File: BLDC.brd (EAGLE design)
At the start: 75.9 x 65.4 mm, 131 parts, among them J3 1-770174-1, U1 MCP2562, U2 STM32F405RGT6, U3 DRV8302, U4 LM3671MF-3.3/NOPB, Y1 8MHz

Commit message: added stm32 LEDs
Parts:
- removed J3: 1-770174-1, FormE:CON4_2X2_P163_VMNL-1MTG
- removed R54, R55: 1k, adafruit:R0805
- added LED4: GREEN, FormE:CHIP-LED0805
- added LED5: RED, FormE:CHIP-LED0805
- added R56, R57: 1k, adafruit:R0805
- moved J5 327.9 mm to (80.3, 61.9)
- moved J4 299.6 mm to (91.8, 50.5)
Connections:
- net LED_RED renamed LED_RED_1
- removed net AUX_10: R55.2, U2.57
- removed net AUX_9: R54.2, U2.56
- removed net LED_GREEN: LED1.A, U2.24
- new net LED_GREEN_1: LED4.A, U2.24
- new net LED_GREEN_2: LED1.A, U2.57
- new net LED_RED_2: LED5.A, U2.56
- new net N$38: LED4.C, R56.2
- new net N$39: LED5.C, R57.2
- net DGND: now also J4.1
- net GND: now also R56.1, R57.1; no longer R54.1, R55.1
- net H1_VS: now also J5.1
- net H2_VS: now also J5.2
- net H3_VS: now also J5.3
- net VCC: now also J4.2
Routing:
- net LED_GREEN_1: track 0.00 -> 1.53 mm, vias 0 -> 1
- net LED_GREEN: track 1.53 -> 0.00 mm, vias 1 -> 0
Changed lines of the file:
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@@
 <attribute name="PARTNO" value="ERJ-6ENF1001V" x="-148.2725" y="-49.2125" size="1.778" layer="27" display="off"/>
-</element>
-<element name="R54" library="adafruit" package="R0805" value="1k" x="-148.2725" y="-54.9275">
-<attribute name="PARTNO" value="ERJ-6ENF1001V" x="-148.2725" y="-54.9275" size="1.778" layer="27" display="off"/>
-</element>
-<element name="R55" library="adafruit" package="R0805" value="1k" x="-148.2725" y="-60.6425">
-<attribute name="PARTNO" value="ERJ-6ENF1001V" x="-148.2725" y="-60.6425" size="1.778" layer="27" display="off"/>
 </element>
 <element name="J6" library="FormE" package="JST-1X7" value="" x="93.6625" y="22.225" rot="R180"/>
@@
 <element name="J1" library="FormE" package="JST-1X7" value="" x="-137.4775" y="-123.5075"/>
 <element name="J2" library="FormE" package="JST-1X7" value="" x="-137.4775" y="-136.8425"/>
-<element name="J3" library="FormE" package="CON4_2X2_P163_VMNL-1MTG" value="1-770174-1" x="-13.6525" y="55.245" rot="R270"/>
-<element name="J4" library="FormE" package="IPBT-102-H1-XX-S-RA" value="" x="-134.62" y="-145.7325"/>
-<element name="J5" library="FormE" package="IPBT-103-H1-XX-S-RA" value="" x="-134.62" y="-185.7375"/>
+<element name="J4" library="FormE" package="IPBT-102-H1-XX-S-RA" value="" x="91.7575" y="50.4825"/>
+<element name="J5" library="FormE" package="IPBT-103-H1-XX-S-RA" value="" x="80.3275" y="61.9125"/>
+<element name="LED4" library="FormE" package="CHIP-LED0805" value="GREEN" x="-147.32" y="-148.59">
+<attribute name="PARTNO" value="598-8170-107F" x="-153.3525" y="-140.0175" size="1.778" layer="27" display="off"/>
+</element>
+<element name="R56" library="adafruit" package="R0805" value="1k" x="-148.2725" y="-154.6225">
+<attribute name="PARTNO" value="ERJ-6ENF1001V" x="-154.305" y="-146.3675" size="1.778" layer="27" display="off"/>
+</element>
+<element name="R57" library="adafruit" package="R0805" value="1k" x="-148.2725" y="-167.3225">
+<attribute name="PARTNO" value="ERJ-6ENF1001V" x="-148.2725" y="-160.3375" size="1.778" layer="27" display="off"/>
+</element>
+<element name="LED5" library="FormE" package="CHIP-LED0805" value="RED" x="-147.32" y="-161.29"/>
 </elements>
 <signals>
@@
 <wire x1="27.785" y1="22.2125" x2="27.785" y2="31.9125" width="0.254" layer="1"/>
 <contactref element="R46" pad="1"/>
-<contactref element="R55" pad="1"/>
-<contactref element="R54" pad="1"/>
 <contactref element="R53" pad="1"/>
 <contactref element="R52" pad="1"/>
@@
 <contactref element="J6" pad="P$1"/>
 <contactref element="J9" pad="P$1"/>
+<contactref element="R56" pad="1"/>
+<contactref element="R57" pad="1"/>
 <wire x1="-143.4775" y1="-96.8375" x2="-143.49" y2="-110.1725" width="0" layer="19" extent="1-1"/>
 <wire x1="-141.4775" y1="-83.5025" x2="-143.4775" y2="-96.8375" width="0" layer="19" extent="1-1"/>
-<wire x1="-149.2725" y1="-60.6425" x2="-141.4775" y2="-83.5025" width="0" layer="19" extent="1-1"/>
-<wire x1="-149.2725" y1="-54.9275" x2="-149.2725" y2="-60.6425" width="0" layer="19" extent="1-1"/>
-<wire x1="-149.2725" y1="-49.2125" x2="-149.2725" y2="-54.9275" width="0" layer="19" extent="1-1"/>
+<wire x1="-149.2725" y1="-49.2125" x2="-141.4775" y2="-83.5025" width="0" layer="19" extent="1-1"/>
 <wire x1="-149.2725" y1="-43.4975" x2="-149.2725" y2="-49.2125" width="0" layer="19" extent="1-1"/>
 <wire x1="-149.2725" y1="-37.7825" x2="-149.2725" y2="-43.4975" width="0" layer="19" extent="1-1"/>
@@
 <wire x1="-149.2725" y1="-14.9225" x2="-149.2725" y2="-20.6375" width="0" layer="19" extent="1-1"/>
 <wire x1="-149.2725" y1="-9.2075" x2="-149.2725" y2="-14.9225" width="0" layer="19" extent="1-1"/>
+<wire x1="-149.2725" y1="-154.6225" x2="-143.49" y2="-110.1725" width="0" layer="19" extent="1-1"/>
+<wire x1="-149.2725" y1="-167.3225" x2="-149.2725" y2="-154.6225" width="0" layer="19" extent="1-1"/>
 <wire x1="-62.23" y1="2.74" x2="-149.2725" y2="-9.2075" width="0" layer="19" extent="1-1"/>
 <wire x1="-60.9" y1="24.64" x2="-62.23" y2="2.74" width="0" layer="19" extent="1-1"/>
@@
 <wire x1="16.145" y1="67.945" x2="17.145" y2="72.805" width="0" layer="19" extent="16-16"/>
 </signal>
-<signal name="LED_GREEN">
-<contactref element="U2" pad="24"/>
-<contactref element="LED1" pad="A"/>
-<wire x1="46.4439" y1="16.76" x2="47.875" y2="16.76" width="0.254" layer="1"/>
-<wire x1="47.875" y1="16.76" x2="47.9425" y2="16.8275" width="0.254" layer="1"/>
-<via x="47.9425" y="16.8275" extent="1-16" drill="0.5"/>
-<wire x1="46.4439" y1="16.76" x2="17.145" y2="70.705" width="0" layer="19" extent="1-16"/>
-</signal>
-<signal name="LED_RED">
-<contactref element="U2" pad="25"/>
-<contactref element="LED2" pad="A"/>
-<wire x1="46.4439" y1="16.26" x2="47.875" y2="16.26" width="0.254" layer="1"/>
-<wire x1="47.875" y1="16.26" x2="47.9425" y2="16.1925" width="0.254" layer="1"/>
-<via x="47.9425" y="16.1925" extent="1-16" drill="0.5"/>
-<wire x1="46.4439" y1="16.26" x2="-147.32" y2="-4.225" width="0" layer="19" extent="1-1"/>
-</signal>
 <signal name="RX_SCL_MOSI">
 <contactref element="U2" pad="38"/>
@@
 <wire x1="20.285" y1="24.4825" x2="19.685" y2="25.0825" width="0.4064" layer="1"/>
 <wire x1="19.685" y1="25.0825" x2="19.05" y2="25.0825" width="0.4064" layer="1"/>
+<contactref element="J4" pad="2"/>
 <wire x1="12.7" y1="27.3075" x2="-135.8265" y2="5.08" width="0" layer="19" extent="1-1"/>
 <wire x1="15.24" y1="27.3075" x2="12.7" y2="27.3075" width="0" layer="19" extent="1-1"/>
@@
 <wire x1="42.2275" y1="58.4327" x2="29.845" y2="58.4327" width="0" layer="19" extent="1-1"/>
 <wire x1="54.61" y1="58.4327" x2="42.2275" y2="58.4327" width="0" layer="19" extent="1-1"/>
+<wire x1="93.853" y1="38.7223" x2="54.61" y2="58.4327" width="0" layer="19" extent="1-1"/>
 </signal>
 <signal name="N$20">
@@
 <wire x1="21.9075" y1="25.7175" x2="21.59" y2="26.035" width="0.254" layer="1"/>
 <wire x1="21.59" y1="26.035" x2="21.59" y2="27.3075" width="0.254" layer="1"/>
+<contactref element="J5" pad="1"/>
+<wire x1="41.5925" y1="37.195" x2="78.232" y2="62.8523" width="0" layer="19" extent="1-1"/>
 <wire x1="32.385" y1="47.825" x2="41.5925" y2="37.195" width="0" layer="19" extent="1-1"/>
 <wire x1="24.285" y1="25.245" x2="41.5925" y2="37.195" width="0" layer="19" extent="1-1"/>
@@
 <wire x1="26.785" y1="29.5275" x2="26.785" y2="31.3175" width="0.254" layer="1"/>
 <wire x1="26.785" y1="31.3175" x2="26.67" y2="31.4325" width="0.254" layer="1"/>
+<contactref element="J5" pad="2"/>
+<wire x1="57.15" y1="47.825" x2="82.423" y2="62.8523" width="0" layer="19" extent="1-1"/>
 <wire x1="43.4975" y1="37.195" x2="57.15" y2="47.825" width="0" layer="19" extent="1-1"/>
 <wire x1="26.785" y1="31.3175" x2="43.4975" y2="37.195" width="0" layer="19" extent="1-1"/>
@@
 <wire x1="30.48" y1="25.7175" x2="31.4325" y2="26.67" width="0.254" layer="1"/>
 <wire x1="31.4325" y1="26.67" x2="31.4325" y2="30.7975" width="0.254" layer="1"/>
+<contactref element="J5" pad="3"/>
+<wire x1="44.7675" y1="47.825" x2="86.614" y2="62.8523" width="0" layer="19" extent="1-1"/>
 <wire x1="45.4025" y1="37.195" x2="44.7675" y2="47.825" width="0" layer="19" extent="1-1"/>
 <wire x1="31.4325" y1="30.7975" x2="45.4025" y2="37.195" width="0" layer="19" extent="1-1"/>
@@
 <signal name="DGND">
 <contactref element="C1" pad="2"/>
+<contactref element="J4" pad="1"/>
+<wire x1="-128.3335" y1="5.08" x2="89.662" y2="38.7223" width="0" layer="19" extent="1-1"/>
 </signal>
 <signal name="N$36">
@@
 <wire x1="57.6961" y1="15.76" x2="-147.2725" y2="-49.2125" width="0" layer="19" extent="1-1"/>
 </signal>
-<signal name="AUX_9">
-<contactref element="U2" pad="56"/>
-<contactref element="R54" pad="2"/>
-<wire x1="57.6961" y1="16.26" x2="-147.2725" y2="-54.9275" width="0" layer="19" extent="1-1"/>
-</signal>
-<signal name="AUX_10">
-<contactref element="U2" pad="57"/>
-<contactref element="R55" pad="2"/>
-<wire x1="57.6961" y1="16.76" x2="-147.2725" y2="-60.6425" width="0" layer="19" extent="1-1"/>
-</signal>
 <signal name="HALL_3_IN">
 <contactref element="J8" pad="P$3"/>
 </signal>
+<signal name="LED_GREEN_1">
+<contactref element="U2" pad="24"/>
+<wire x1="46.4439" y1="16.76" x2="47.875" y2="16.76" width="0.254" layer="1"/>
+<wire x1="47.875" y1="16.76" x2="47.9425" y2="16.8275" width="0.254" layer="1"/>
+<via x="47.9425" y="16.8275" extent="1-16" drill="0.5"/>
+<contactref element="LED4" pad="A"/>
+<wire x1="-147.32" y1="-149.64" x2="46.4439" y2="16.76" width="0" layer="19" extent="1-1"/>
+</signal>
+<signal name="LED_RED_1">
+<contactref element="U2" pad="25"/>
+<wire x1="46.4439" y1="16.26" x2="47.875" y2="16.26" width="0.254" layer="1"/>
+<wire x1="47.875" y1="16.26" x2="47.9425" y2="16.1925" width="0.254" layer="1"/>
+<via x="47.9425" y="16.1925" extent="1-16" drill="0.5"/>
+<contactref element="LED2" pad="A"/>
+<wire x1="46.4439" y1="16.26" x2="-147.32" y2="-4.225" width="0" layer="19" extent="1-1"/>
+</signal>
+<signal name="LED_GREEN_2">
+<contactref element="U2" pad="57"/>
+<contactref element="LED1" pad="A"/>
+<wire x1="57.6961" y1="16.76" x2="17.145" y2="70.705" width="0" layer="19" extent="1-16"/>
+</signal>
+<signal name="LED_RED_2">
+<contactref element="U2" pad="56"/>
+<contactref element="LED5" pad="A"/>
+<wire x1="-147.32" y1="-162.34" x2="57.6961" y2="16.26" width="0" layer="19" extent="1-1"/>
+</signal>
+<signal name="N$38">
+<contactref element="R56" pad="2"/>
+<contactref element="LED4" pad="C"/>
+<wire x1="-147.32" y1="-147.54" x2="-147.2725" y2="-154.6225" width="0" layer="19" extent="1-1"/>
+</signal>
+<signal name="N$39">
+<contactref element="R57" pad="2"/>
+<contactref element="LED5" pad="C"/>
+<wire x1="-147.32" y1="-160.24" x2="-147.2725" y2="-167.3225" width="0" layer="19" extent="1-1"/>
+</signal>
 </signals>

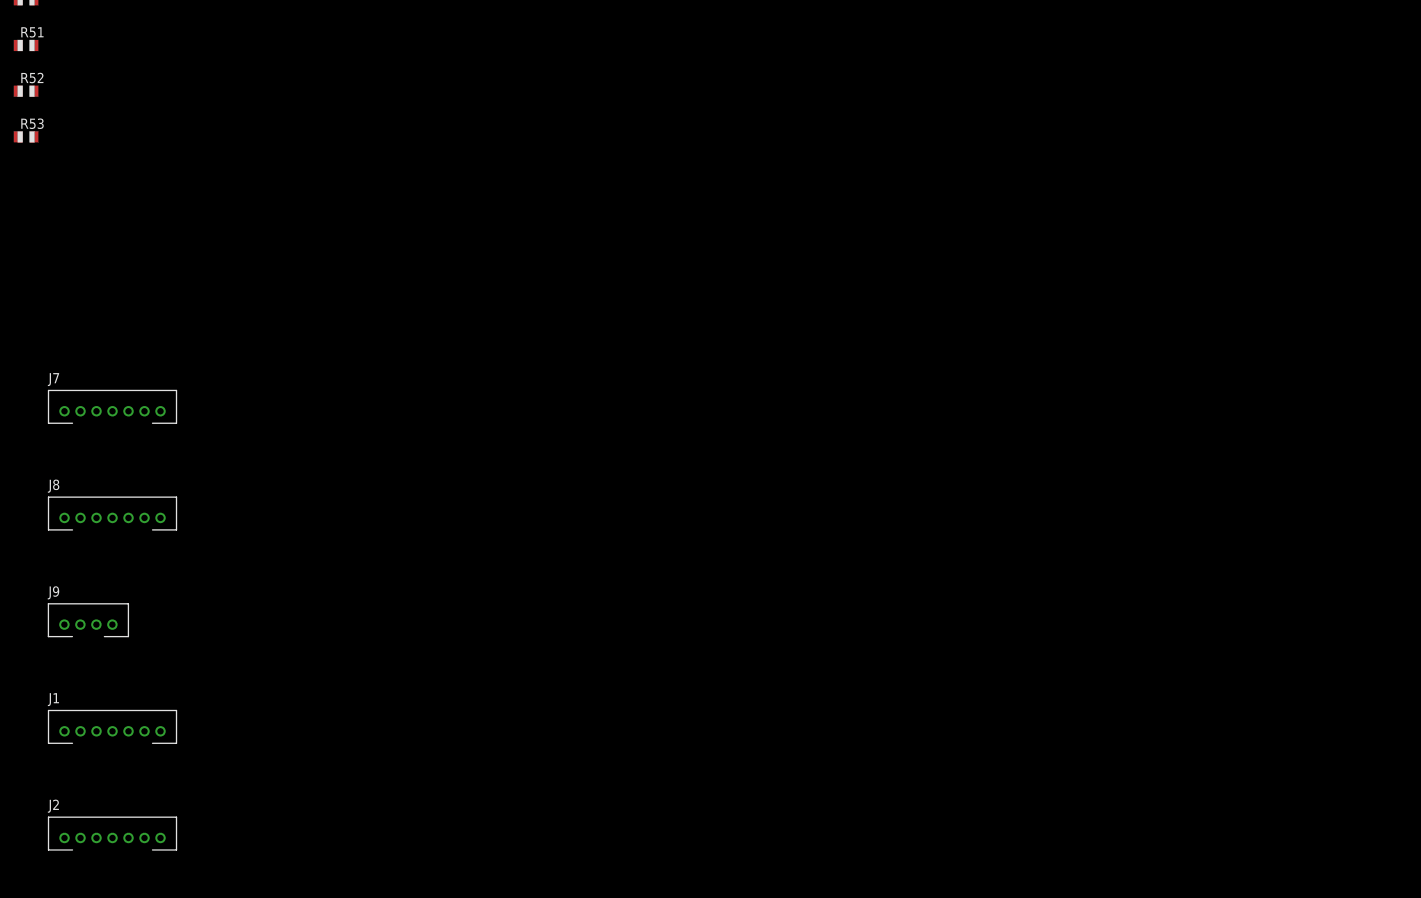
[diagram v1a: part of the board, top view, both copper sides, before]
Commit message: only 8 aux now
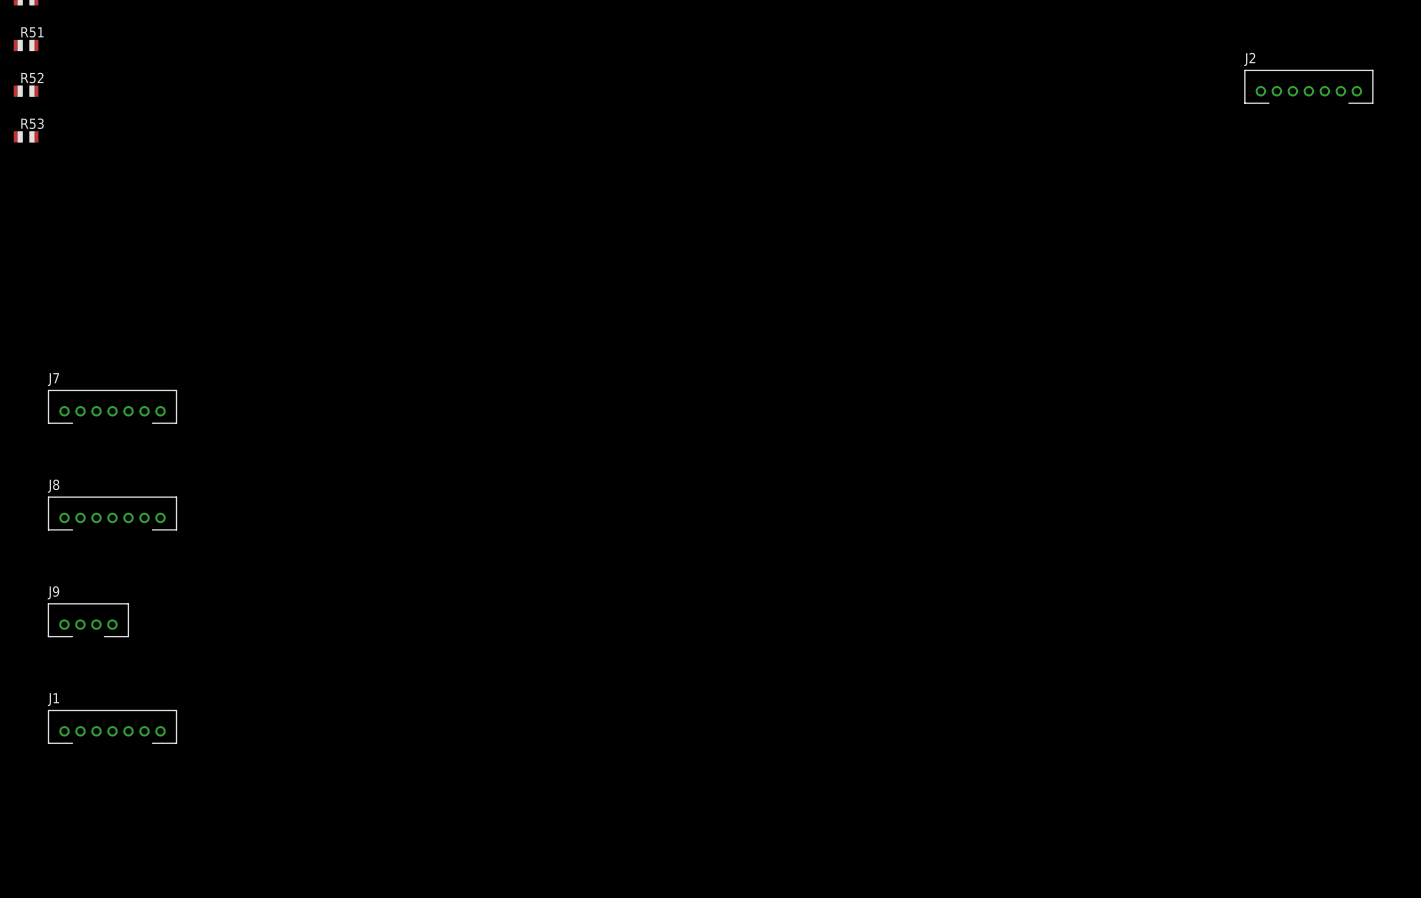
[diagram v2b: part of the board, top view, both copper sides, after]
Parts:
- moved J2 176.3 mm to (12.1, -43.5)
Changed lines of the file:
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@@
 <element name="J9" library="FormE" package="JST-1X4" value="" x="-143.51" y="-110.1725"/>
 <element name="J1" library="FormE" package="JST-1X7" value="" x="-137.4775" y="-123.5075"/>
-<element name="J2" library="FormE" package="JST-1X7" value="" x="-137.4775" y="-136.8425"/>
+<element name="J2" library="FormE" package="JST-1X7" value="" x="12.065" y="-43.4975"/>
 <element name="J4" library="FormE" package="IPBT-102-H1-XX-S-RA" value="" x="91.7575" y="50.4825"/>
 <element name="J5" library="FormE" package="IPBT-103-H1-XX-S-RA" value="" x="80.3275" y="61.9125"/>

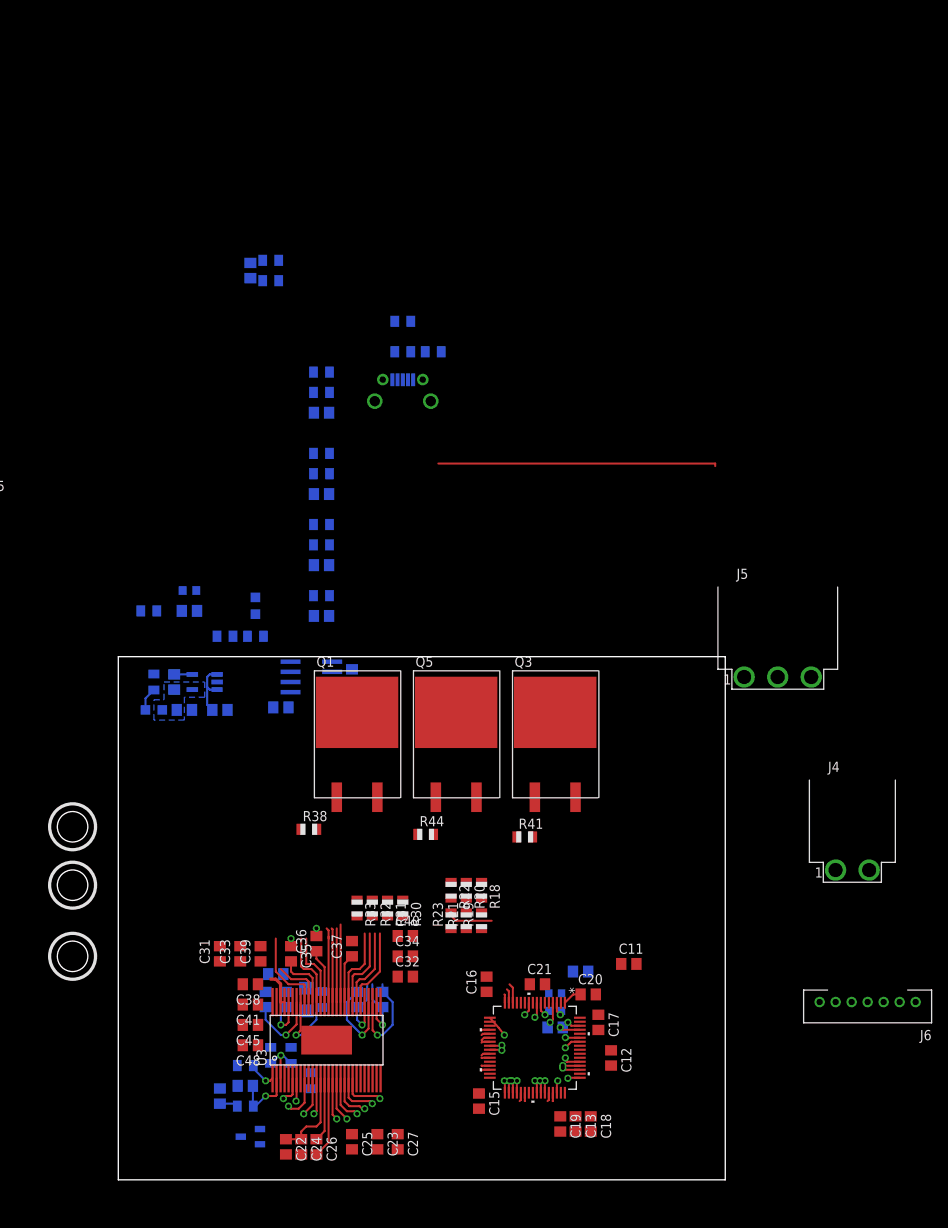
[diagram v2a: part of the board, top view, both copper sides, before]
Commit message: about to change fet driver module
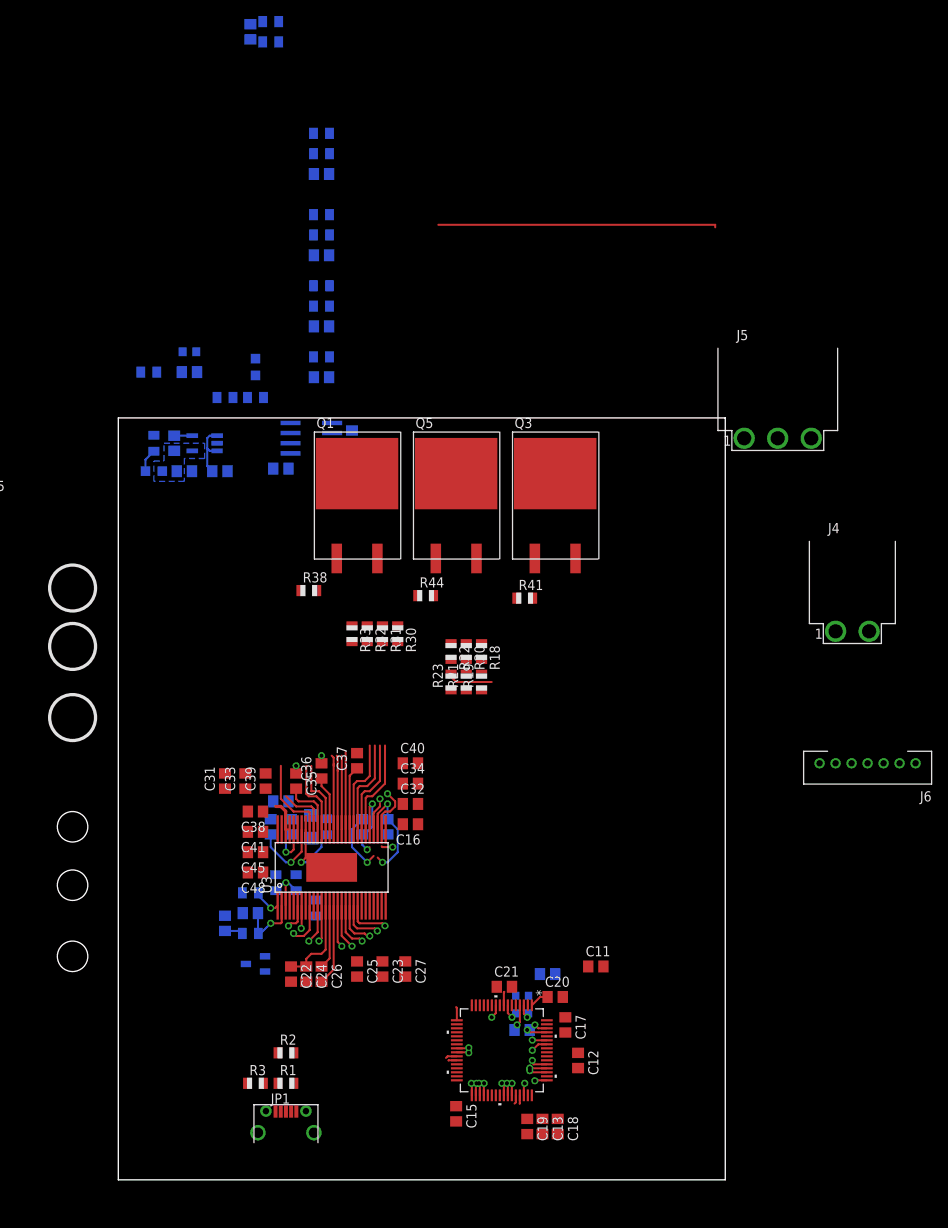
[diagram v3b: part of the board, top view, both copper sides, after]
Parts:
- moved R3 94.1 mm to (17.1, 12.1), flipped to the top
- moved JP1 92.6 mm to (21.0, 5.71), flipped to the top
- moved R1 92.6 mm to (21.0, 12.1), flipped to the top
- moved R2 92.6 mm to (21.0, 15.9), flipped to the top
- moved R30 34.3 mm to (34.9, 68.3)
- moved R31 34.3 mm to (33.0, 68.3)
- moved R32 34.3 mm to (31.1, 68.3)
- moved R33 34.3 mm to (29.2, 68.3)
- moved C5 29.8 mm to (25.4, 106.7)
- moved R13 29.8 mm to (19.1, 142.2)
- moved R14 29.8 mm to (17.1, 97.8)
- moved R15 29.8 mm to (13.3, 97.8)
- moved R9 29.8 mm to (25.4, 128.3)
- moved C7 29.8 mm to (20.3, 88.9)
- moved L1 29.8 mm to (6.99, 92.1)
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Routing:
- net TX_SDA_NSS: track 3.24 -> 0.00 mm
- net RX_SCL_MOSI: track 3.19 -> 0.00 mm
- net SENS3: track 8.20 -> 5.71 mm
- net N$27: track 6.11 -> 8.02 mm
- net M_L3: track 9.90 -> 11.8 mm
- net M_H3: track 9.98 -> 11.9 mm
- net H3_VS: track 10.0 -> 11.9 mm
- net H3_LOW: track 9.96 -> 11.9 mm
- net SENS2: track 1.78 -> 0.00 mm
- net N$28: track 8.94 -> 7.33 mm, vias 1 -> 2
- net N$24: track 9.03 -> 10.4 mm, vias 1 -> 2
- net MISO_ADC_EXT2: track 1.16 -> 0.00 mm
- net ADC_TEMP: track 2.83 -> 1.68 mm, vias 1 -> 0
- net SCK_ADC_EXT: track 1.11 -> 0.00 mm
- net SENS1: track 1.10 -> 0.03 mm
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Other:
- board size 75.9 x 65.4 mm -> 75.9 x 95.2 mm
